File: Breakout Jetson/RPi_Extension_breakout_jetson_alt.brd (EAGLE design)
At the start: 63 x 70.1 mm, 9 parts, among them U1 CD74HC137_PW_16, U2 CD74HC137_PW_16

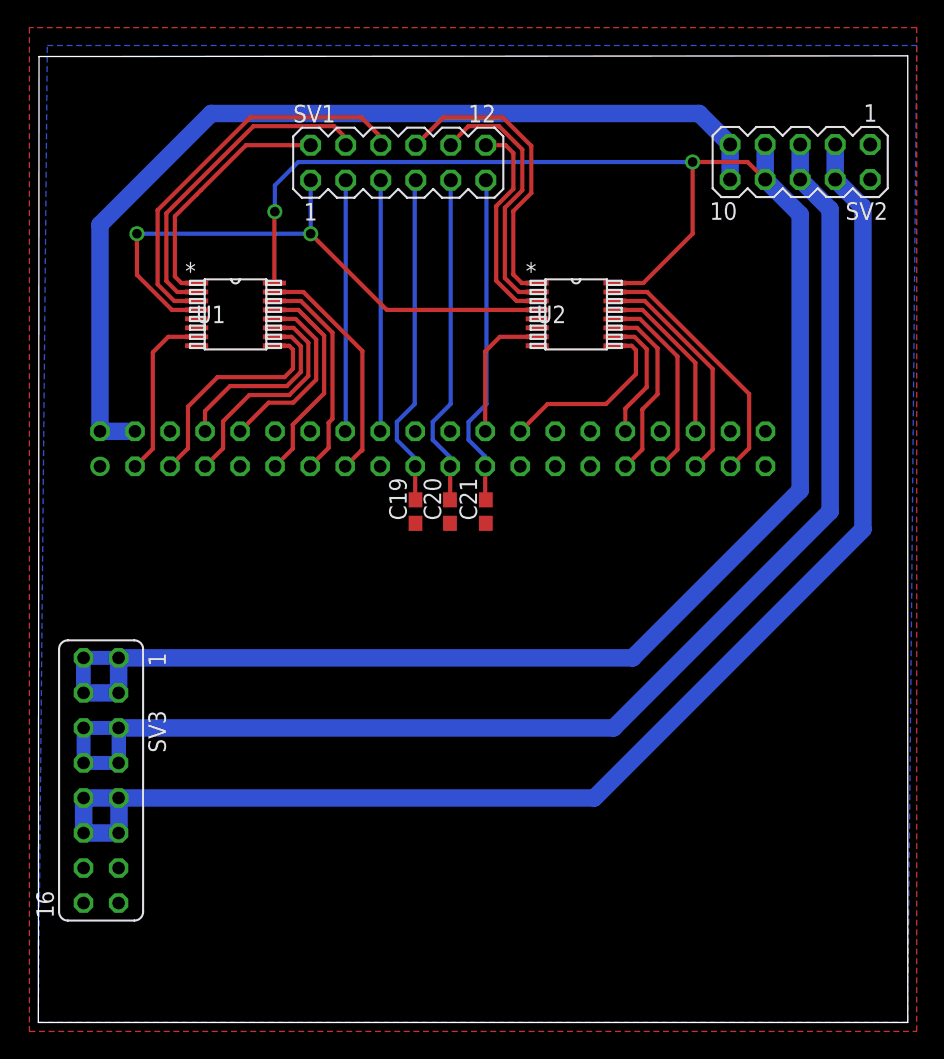
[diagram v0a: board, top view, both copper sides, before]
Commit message: added additional jetson breakout board just using one 1:16 multiplexer
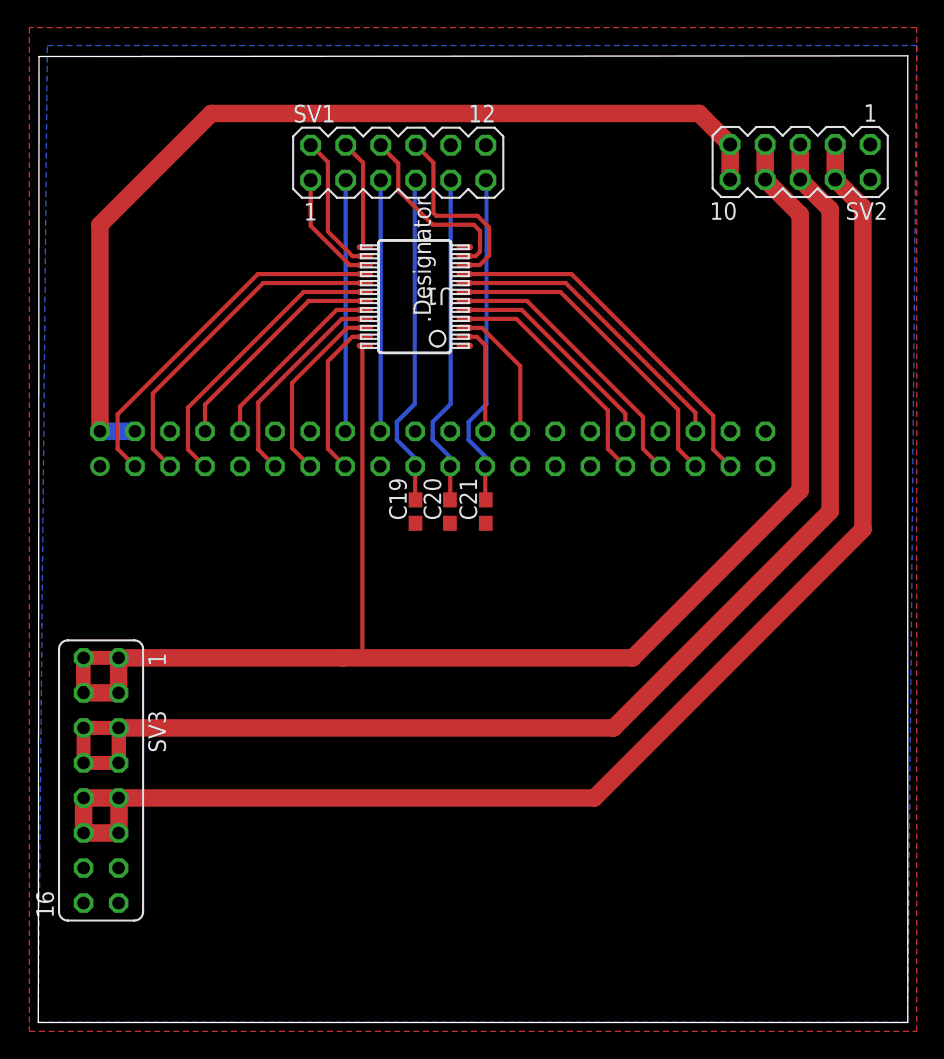
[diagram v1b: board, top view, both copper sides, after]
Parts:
- removed U2: CD74HC137_PW_16, CD74HC137:PW16
- U1: value CD74HC137_PW_16 -> (none); device CD74HC137:PW16 -> CD74HC4067:DB0024A_N
- moved U1 13.1 mm to (27.3, 52.6), turned to 180 degrees
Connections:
- removed net LATCH: SV1.1, U1.4, U1.5, U2.4, U2.5
- removed net N$1: U1.6
- new net EN_MULT: SV1.1, U1.15
- net ADDR0: now also U1.14; no longer U1.1
- net ADDR1: now also U1.13; no longer U1.2
- net ADDR2: now also U1.11; no longer U1.3
- net ADDR3: now also U1.10; no longer U2.1
- net ADDR4: no longer U2.2
- net ADDR5: no longer U2.3
- net DVCC: now also U1.24; no longer U1.16, U2.16
- net GND: now also U1.12; no longer U1.8, U2.6, U2.8
- net GPIO0: now also U1.2; no longer U2.7
- net GPIO1: now also U1.3; no longer U2.9
- net GPIO10: now also U1.6; no longer U2.12
- net GPIO11: now also U1.4; no longer U2.11
- net GPIO12: now also U1.16; no longer U1.7
- net GPIO13: now also U1.17; no longer U1.9
- net GPIO14: now also U1.20; no longer U1.12
- net GPIO15: now also U1.19; no longer U1.10
- net GPIO2: now also U1.5; no longer U2.10
- net GPIO3: now also U1.8; no longer U2.13
- net GPIO4: now also U1.18; no longer U1.11
- net GPIO5: now also U1.21; no longer U1.13
- net GPIO6: now also U1.22; no longer U1.14
- net GPIO7: now also U1.23; no longer U1.15
- net GPIO8: now also U1.9; no longer U2.15
- net GPIO9: now also U1.7; no longer U2.14
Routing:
- net LATCH: track 43.6 -> 0.00 mm, vias 2 -> 0
- net DVCC: track 149.2 -> 117.1 mm, vias 2 -> 3
- net ADDR4: track 19.1 -> 0.00 mm
- net ADDR1: track 24.0 -> 7.97 mm
- net ADDR5: track 15.6 -> 0.00 mm
- net ADDR2: track 28.9 -> 13.7 mm
- net GPIO12: track 12.5 -> 26.4 mm
- net GPIO3: track 12.4 -> 22.0 mm
- net EN_MULT: track 0.00 -> 8.41 mm
- net GPIO13: track 16.5 -> 24.5 mm
- net ADDR0: track 18.1 -> 10.2 mm
- net ADDR3: track 21.9 -> 14.0 mm
- net GPIO8: track 18.6 -> 26.5 mm
- net GPIO9: track 16.7 -> 23.6 mm
- net GPIO2: track 9.27 -> 16.0 mm
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
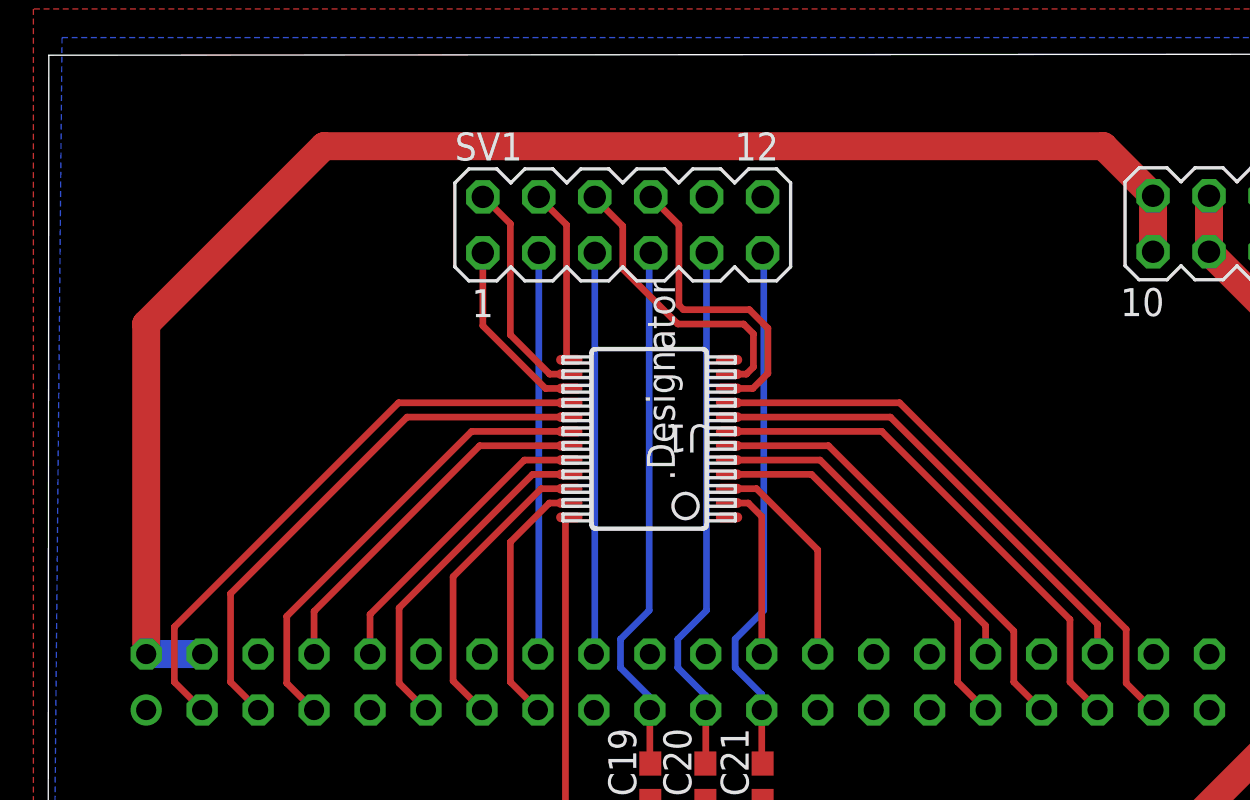
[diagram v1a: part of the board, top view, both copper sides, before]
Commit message: updated package of 1:16 multiplexer
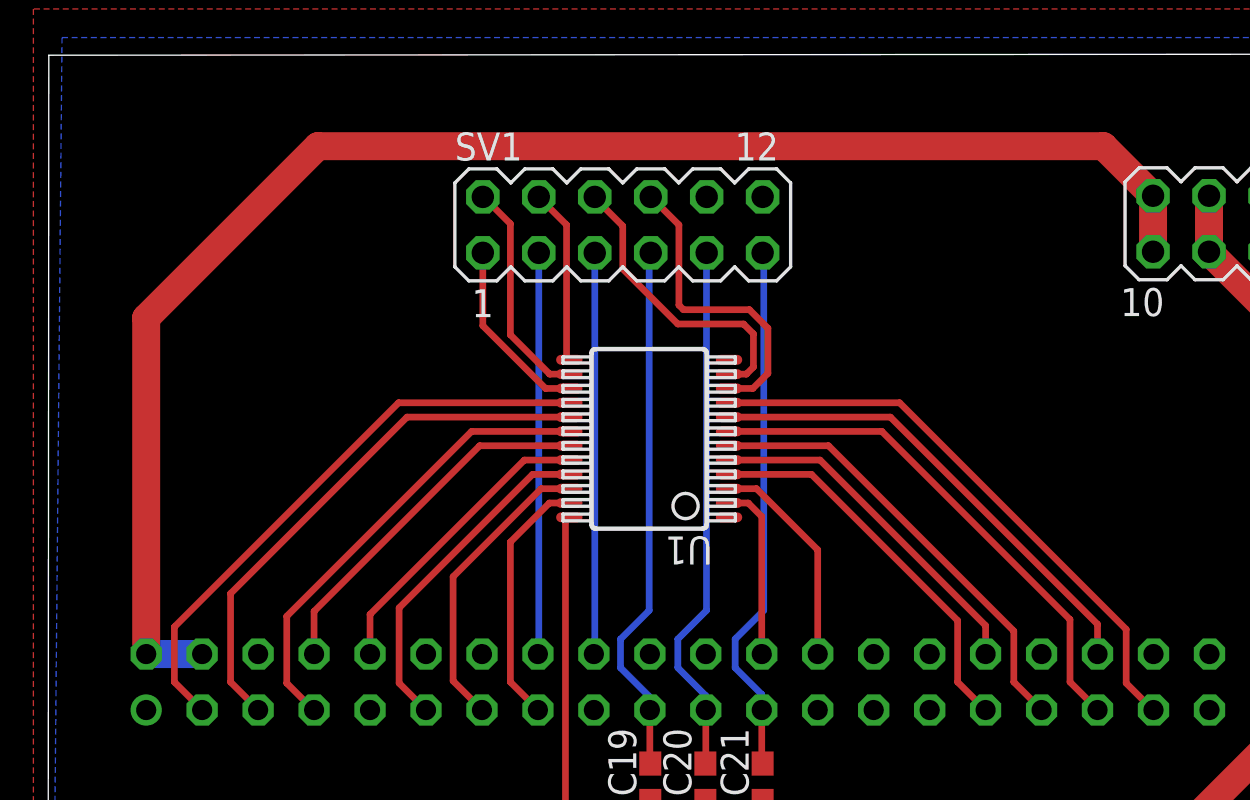
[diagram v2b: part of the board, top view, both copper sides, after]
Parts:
- U1: value (none) -> Value
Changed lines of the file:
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@@
 <attribute name="OC_FARNELL" value="unknown" x="26.1" y="62.35" size="1.778" layer="27" display="off"/>
 </element>
-<element name="U1" library="CD74HC4067" package="DB0024A_N" value="" x="27.3" y="52.65" rot="R180">
+<element name="U1" library="CD74HC4067" package="DB0024A_N" value="Value" x="27.3" y="52.65" rot="R180">
 <attribute name="TYPE" value="TYPE" x="27.3" y="52.65" size="1.778" layer="27" rot="R180" display="off"/>
 <attribute name="MANUFACTURER" value="Texas Instruments" x="27.3" y="52.65" size="1.778" layer="27" rot="R180" display="off"/>
@@
 <wire x1="50.17" y1="63.67" x2="50.17" y2="61.13" width="1.27" layer="1"/>
 <wire x1="50.17" y1="63.67" x2="47.918590625" y2="65.921409375" width="1.27" layer="1"/>
-<wire x1="47.918590625" y1="65.921409375" x2="12.53853125" y2="65.921409375" width="1.27" layer="1"/>
-<wire x1="12.53853125" y1="65.921409375" x2="4.47" y2="57.852878125" width="1.27" layer="1"/>
-<wire x1="4.47" y1="57.852878125" x2="4.47" y2="42.87" width="1.27" layer="1"/>
+<wire x1="47.918590625" y1="65.921409375" x2="12.26083125" y2="65.921409375" width="1.27" layer="1"/>
+<wire x1="12.26083125" y1="65.921409375" x2="4.47" y2="58.130578125" width="1.27" layer="1"/>
+<wire x1="4.47" y1="58.130578125" x2="4.47" y2="42.87" width="1.27" layer="1"/>
 <wire x1="4.47" y1="42.87" x2="7.01" y2="42.87" width="1.27" layer="16"/>
 </signal>

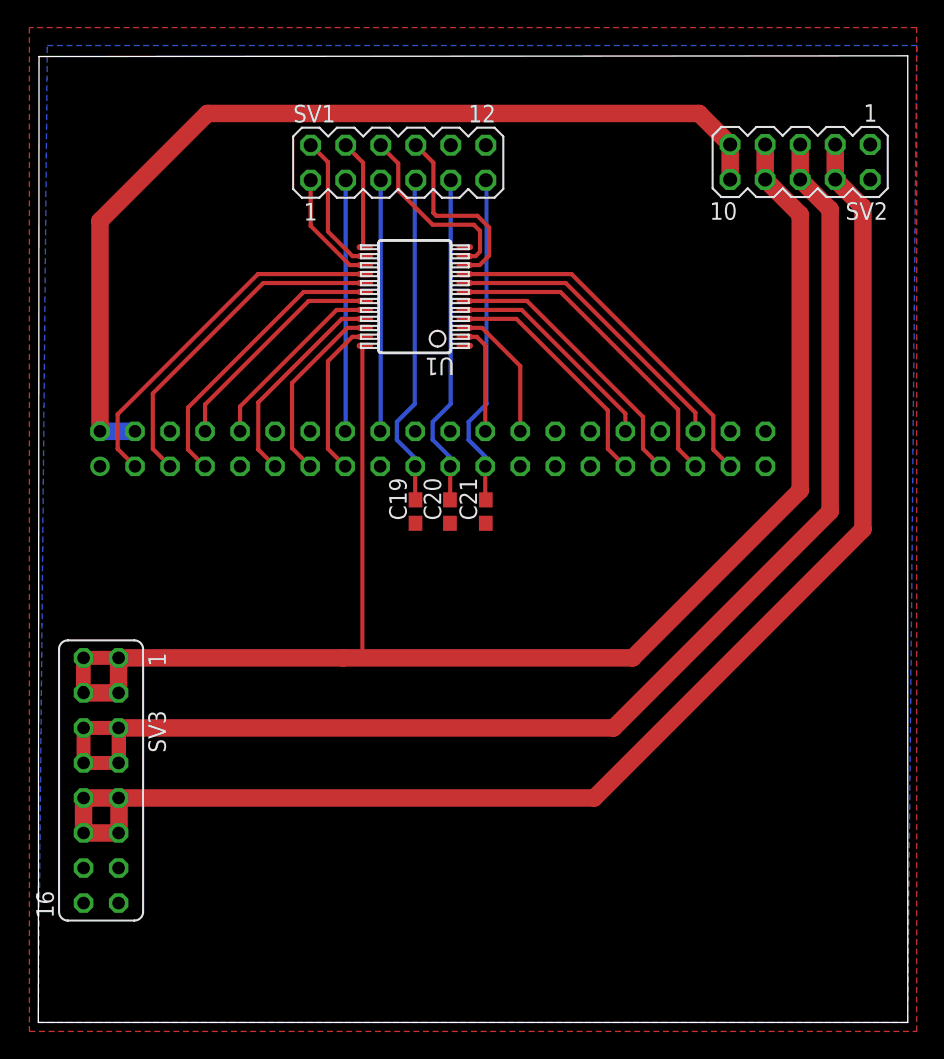
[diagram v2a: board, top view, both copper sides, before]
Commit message: added inverters to jetson tx1 board
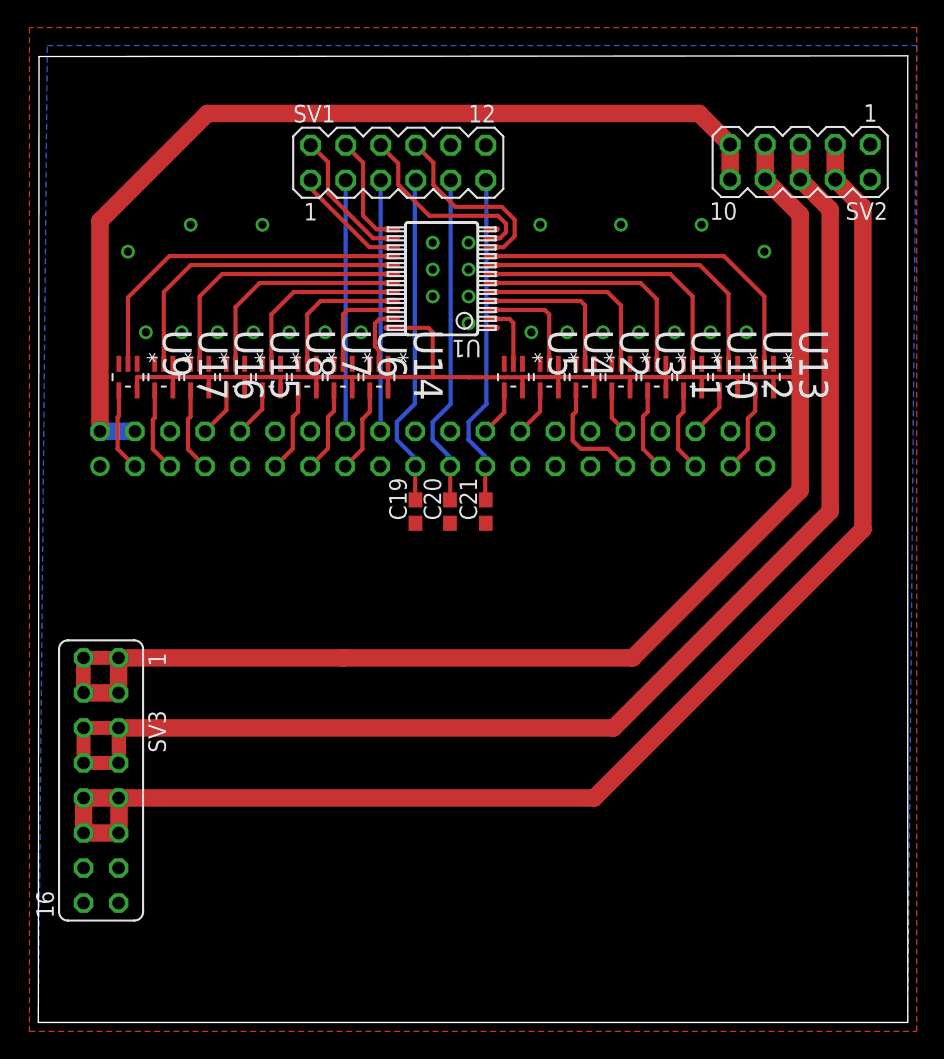
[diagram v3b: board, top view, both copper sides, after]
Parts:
- added U10, U11, U12, U13, U14, U15, U16, U17, U2, U3, U4, U5, U6, U7, U8, U9: 74AHC1G04GW/T1, 74AHC1G04GW:SOT65P210X110-5N
- moved U1 2.34 mm to (29.2, 54.0)
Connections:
- new net GPIO0_NEG: SV5.24, U5.4
- new net GPIO10_NEG: SV5.33, U11.4
- new net GPIO11_NEG: SV5.31, U2.4
- new net GPIO12_NEG: SV5.3, U9.4
- new net GPIO13_NEG: SV5.5, U17.4
- new net GPIO14_NEG: SV5.10, U8.4
- new net GPIO15_NEG: SV5.8, U15.4
- new net GPIO1_NEG: SV5.26, U4.4
- new net GPIO2_NEG: SV5.32, U3.4
- new net GPIO3_NEG: SV5.36, U12.4
- new net GPIO4_NEG: SV5.7, U16.4
- new net GPIO5_NEG: SV5.11, U7.4
- new net GPIO6_NEG: SV5.13, U6.4
- new net GPIO7_NEG: SV5.15, U14.4
- new net GPIO8_NEG: SV5.37, U13.4
- new net GPIO9_NEG: SV5.35, U10.4
- net DVCC: now also U10.5, U11.5, U12.5, U13.5, U14.5, U15.5, U16.5, U17.5, U2.5, U3.5, U4.5, U5.5, U6.5, U7.5, U8.5, U9.5
- net GND: now also U10.3, U11.3, U12.3, U13.3, U14.3, U15.3, U16.3, U17.3, U2.3, U3.3, U4.3, U5.3, U6.3, U7.3, U8.3, U9.3
- net GPIO0: now also U5.2; no longer SV5.24
- net GPIO1: now also U4.2; no longer SV5.26
- net GPIO10: now also U11.2; no longer SV5.33
- net GPIO11: now also U2.2; no longer SV5.31
- net GPIO12: now also U9.2; no longer SV5.3
- net GPIO13: now also U17.2; no longer SV5.5
- net GPIO14: now also U8.2; no longer SV5.10
- net GPIO15: now also U15.2; no longer SV5.8
- net GPIO2: now also U3.2; no longer SV5.32
- net GPIO3: now also U12.2; no longer SV5.36
- net GPIO4: now also U16.2; no longer SV5.7
- net GPIO5: now also U7.2; no longer SV5.11
- net GPIO6: now also U6.2; no longer SV5.13
- net GPIO7: now also U14.2; no longer SV5.15
- net GPIO8: now also U13.2; no longer SV5.37
- net GPIO9: now also U10.2; no longer SV5.35
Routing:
- net DVCC: track 117.1 -> 169.6 mm
- net GPIO11_NEG: track 0.00 -> 8.33 mm
- net GPIO7: track 11.6 -> 4.39 mm
- net GPIO11: track 17.7 -> 11.1 mm
- net GPIO6: track 13.5 -> 7.24 mm
- net GPIO8_NEG: track 0.00 -> 6.25 mm
- net GPIO7_NEG: track 0.00 -> 6.25 mm
- net GPIO6_NEG: track 0.00 -> 6.22 mm
- net GPIO5_NEG: track 0.00 -> 6.20 mm
- net GPIO9_NEG: track 0.00 -> 6.18 mm
- net GPIO10_NEG: track 0.00 -> 6.17 mm
- net GPIO4_NEG: track 0.00 -> 6.10 mm
- net GPIO13_NEG: track 0.00 -> 6.08 mm
- net GPIO12_NEG: track 0.00 -> 6.06 mm
- net GPIO5: track 15.4 -> 10.1 mm
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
